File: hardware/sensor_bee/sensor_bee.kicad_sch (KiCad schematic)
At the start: 8 parts, among them J1 USB_C_Receptacle_USB2.0, SW1 SW_Push, U1 ESP32-C6, U2 AT25DF041x-UxN-x, U3 HDC1080, U4 BME680

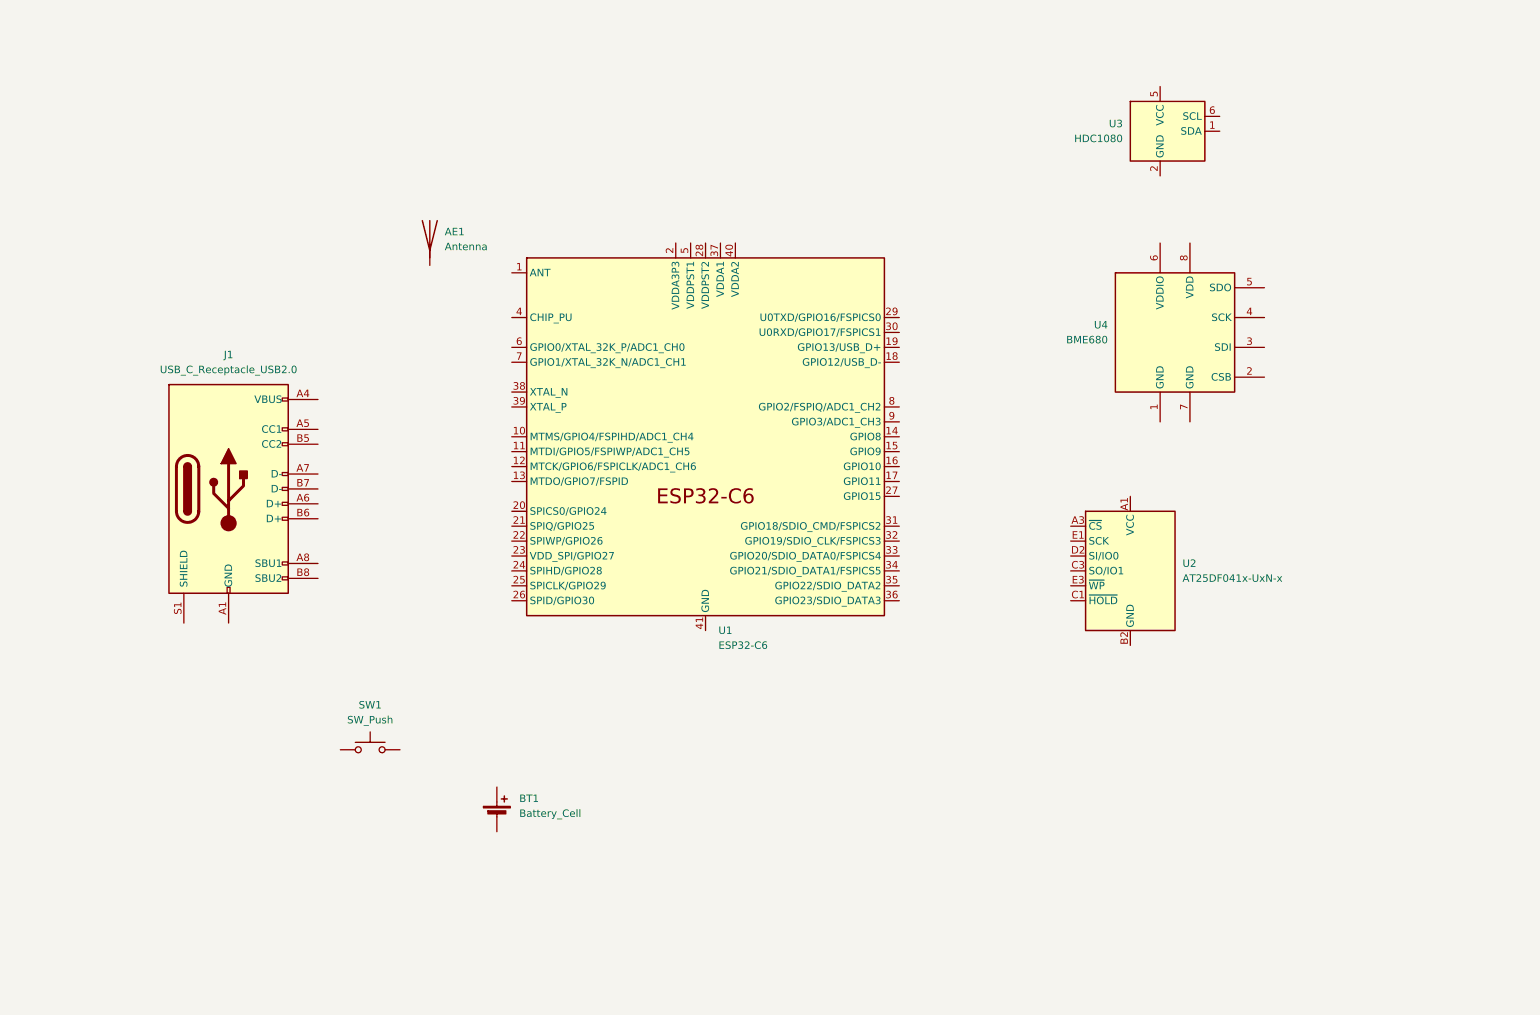
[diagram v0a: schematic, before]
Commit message: Added power supply bypassing & references to readme
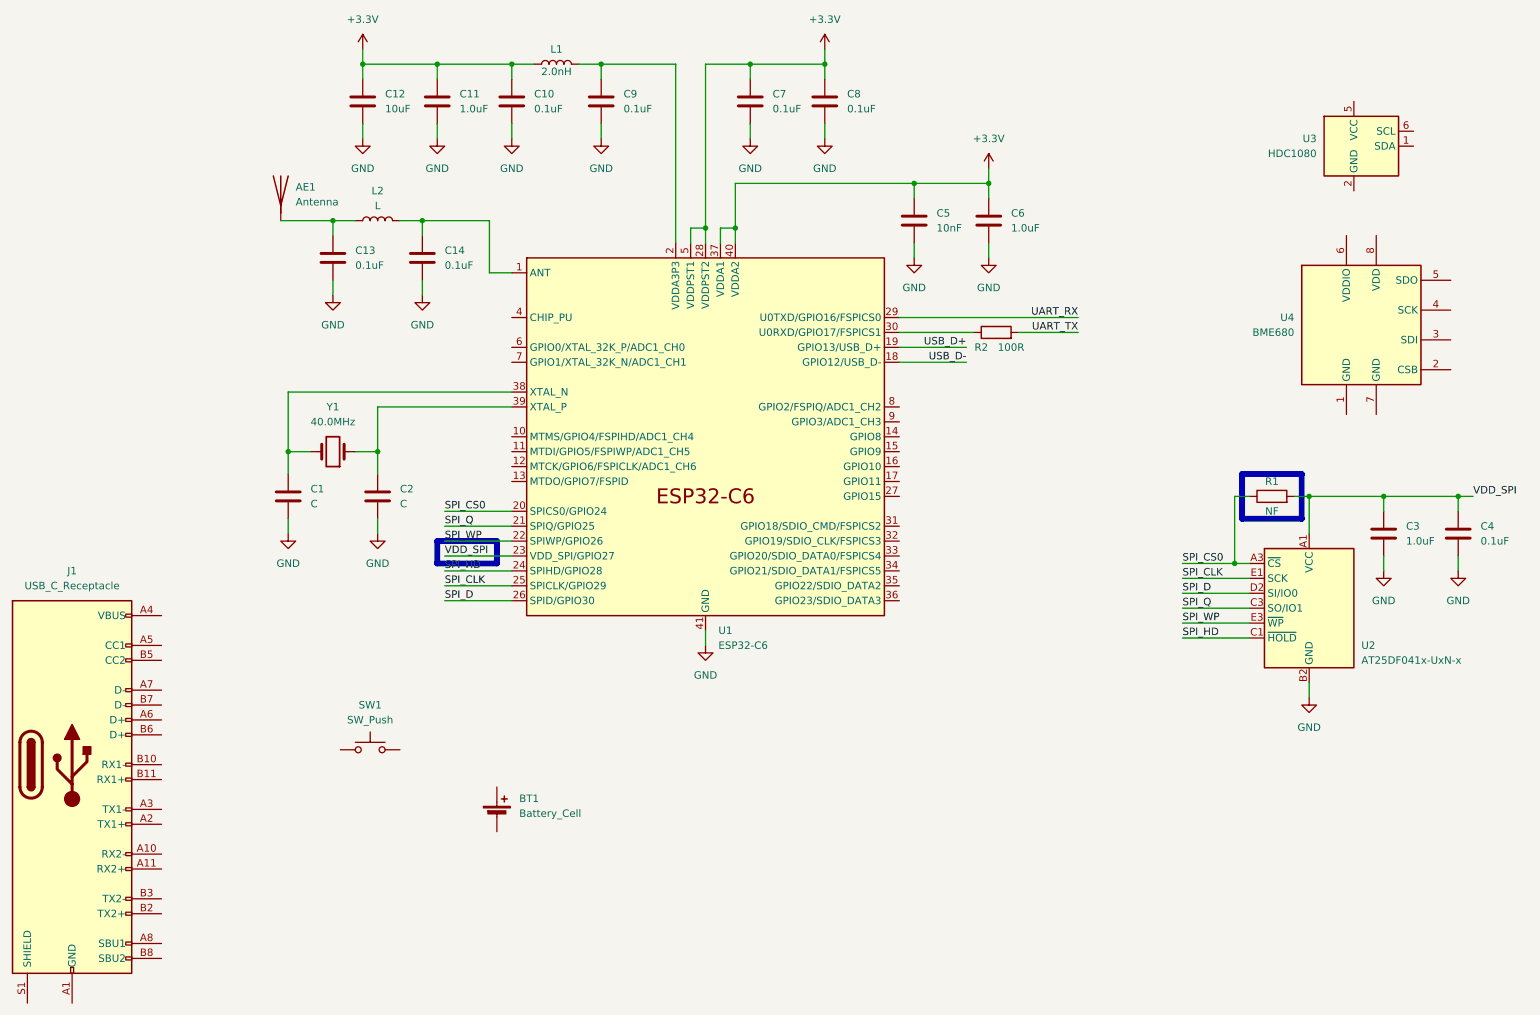
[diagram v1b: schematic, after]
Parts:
- removed J1: USB_C_Receptacle_USB2.0, symbol Connector:USB_C_Receptacle_USB2.0
- added C1, C2: C, symbol Device:C
- added C10, C13, C14, C4, C7, C8, C9: 0.1uF, symbol Device:C
- added C11, C3, C6: 1.0uF, symbol Device:C
- added C12: 10uF, symbol Device:C
- added C5: 10nF, symbol Device:C
- added J1: USB_C_Receptacle, symbol Connector:USB_C_Receptacle
- added L1: 2.0nH, symbol Device:L
- added L2: L, symbol Device:L
- added R1: NF, symbol Device:R
- added R2: 100R, symbol Device:R
- added Y1: 40.0MHz, symbol Device:Crystal
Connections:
- net at U1.1 (ANT): now also C14.1, L2.2
- net USB_D-: now reaches U1.18 (GPIO12/USB_D-)
- net USB_D+: now reaches U1.19 (GPIO13/USB_D+)
- net at U1.2 (VDDA3P3), U1.3 (VDDA3P3): now also C9.1, L1.2
- net SPI_CS0: now reaches U1.20 (SPICS0/GPIO24)
- net SPI_CS0: now also U2.A3 (~{CS}), R1.1
- net SPI_Q: now reaches U1.21 (SPIQ/GPIO25)
- net SPI_Q: now also U2.C3 (SO/IO1)
- net SPI_WP: now reaches U1.22 (SPIWP/GPIO26)
- net SPI_WP: now also U2.E3 (~{WP})
- net VDD_SPI: now reaches U1.23 (VDD_SPI/GPIO27)
- net VDD_SPI: now also U2.A1 (VCC), C3.1, C4.1, R1.2
- net SPI_HD: now reaches U1.24 (SPIHD/GPIO28)
- net SPI_HD: now also U2.C1 (~{HOLD})
- net SPI_CLK: now reaches U1.25 (SPICLK/GPIO29)
- net SPI_CLK: now also U2.E1 (SCK)
- net SPI_D: now reaches U1.26 (SPID/GPIO30)
- net SPI_D: now also U2.D2 (SI/IO0)
- net +3.3V: now reaches U1.28 (VDDPST2)
- net +3.3V: now also U1.37 (VDDA1), U1.40 (VDDA2), U1.5 (VDDPST1), C10.1, C11.1, C12.1, C5.1, C6.1, C7.1, C8.1, L1.1
- net UART_RX: now reaches U1.29 (U0TXD/GPIO16/FSPICS0)
- net at U1.30 (U0RXD/GPIO17/FSPICS1): now also R2.1
- net at U1.38 (XTAL_N): now also C1.1, Y1.2
- net at U1.39 (XTAL_P): now also C2.1, Y1.1
- net GND: now reaches U1.41 (GND)
- net GND: now also U2.B2 (GND), C1.2, C10.2, C11.2, C12.2, C13.2, C14.2, C2.2, C3.2, C4.2, C5.2, C6.2, C7.2, C8.2, C9.2
- net at AE1.1 (A): now also C13.1, L2.1
- new net: J1.A1 (GND), J1.A12 (GND), J1.B1 (GND), J1.B12 (GND)
- new net: J1.A4 (VBUS), J1.A9 (VBUS), J1.B4 (VBUS), J1.B9 (VBUS)
- new net UART_TX: R2.2
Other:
- moved on the sheet: AE1, U2, U3, U4
